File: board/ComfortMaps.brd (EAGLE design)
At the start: 96.8 x 49.3 mm, 47 parts, among them J1 PROG_HDR, U1 ADXL362, U3 ADP160-3.3, U4 MCP73833, X1 RASPI_GPIO_B+#_PIN

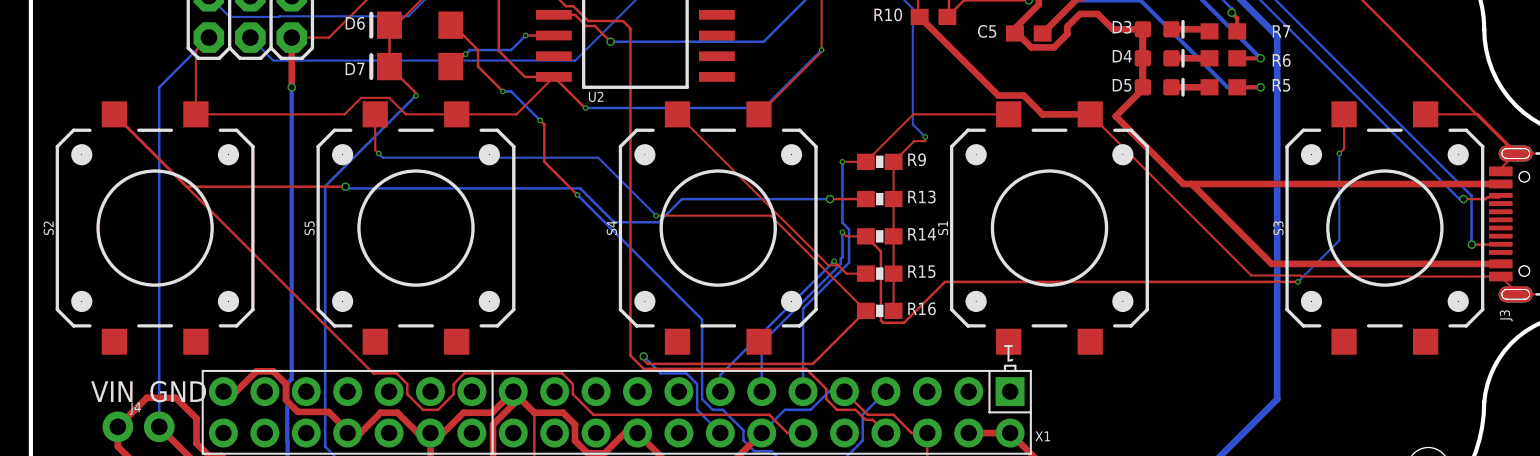
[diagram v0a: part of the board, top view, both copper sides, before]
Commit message: Enlarging spst button pads and connecting both sides.
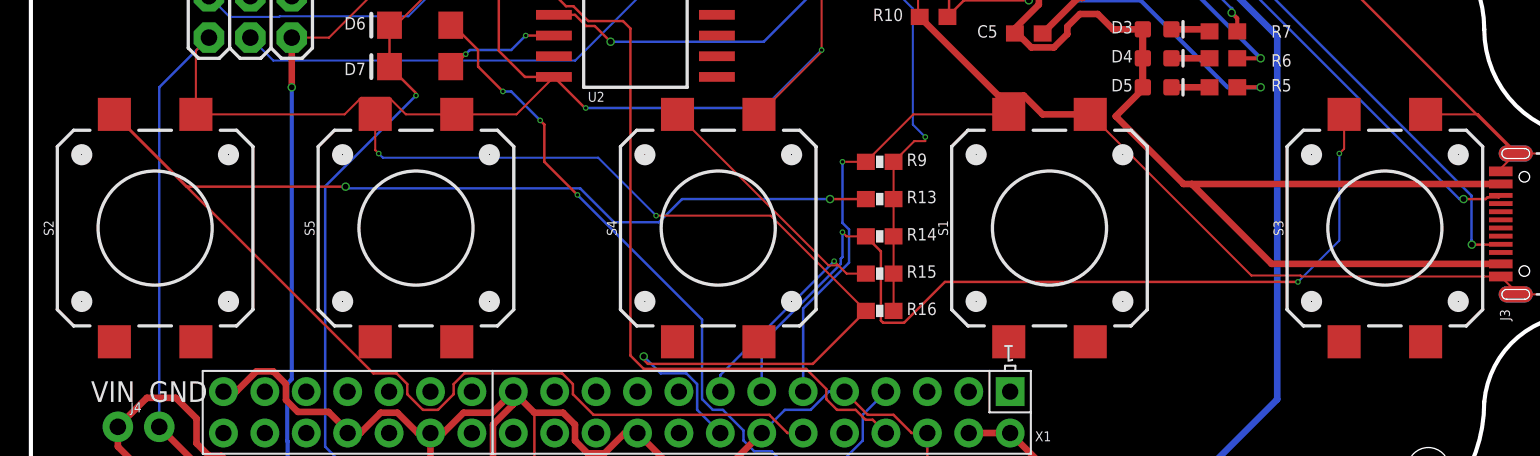
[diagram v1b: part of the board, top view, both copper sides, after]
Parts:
- S1, S2, S3, S4, S5: device SparkFun-Switches:TACTILE_SWITCH_SMD_12MM -> CM-SparkFun-Switches:TACTILE_SWITCH_SMD_12MM
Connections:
- net GND: now also S1.2, S2.2, S3.2, S4.2, S5.2
- net GPIO17: now also S1.4
- net GPIO18: now also S2.4
- net GPIO22: now also S4.4
- net GPIO23: now also S5.4
- net GPIO27: now also S3.4
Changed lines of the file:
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@@
 </element>
 <element name="U$3" library="SparkFun-Aesthetics" package="OSHW-LOGO-S" value="" x="6.274" y="0.279" smashed="yes" rot="R90"/>
-<element name="S1" library="SparkFun-Switches" library_urn="urn:adsk.eagle:library:535" package="TACTILE_SWITCH_SMD_12MM" package3d_urn="urn:adsk.eagle:package:40166/1" value="SPST-12MM" x="66.294" y="18.542" smashed="yes" rot="R90">
+<element name="S1" library="CM-SparkFun-Switches" package="TACTILE_SWITCH_SMD_12MM" value="SPST-12MM" x="66.294" y="18.542" smashed="yes" rot="R90">
 <attribute name="NAME" x="60.071" y="18.542" size="0.6096" layer="25" font="vector" ratio="20" rot="R90" align="bottom-center"/>
 <attribute name="PROD_ID" value="SWCH-11967" x="66.294" y="18.542" size="1.778" layer="27" rot="R90" display="off"/>
@@
 <attribute name="VALUE" x="72.517" y="18.542" size="0.6096" layer="27" font="vector" ratio="20" rot="R90" align="top-center"/>
 </element>
-<element name="S2" library="SparkFun-Switches" library_urn="urn:adsk.eagle:library:535" package="TACTILE_SWITCH_SMD_12MM" package3d_urn="urn:adsk.eagle:package:40166/1" override_package3d_urn="urn:adsk.eagle:package:15371983/2" override_package_urn="urn:adsk.eagle:footprint:40109/1" value="SPST-12MM" x="11.43" y="18.542" smashed="yes" rot="R90">
+<element name="S2" library="CM-SparkFun-Switches" package="TACTILE_SWITCH_SMD_12MM" override_package3d_urn="urn:adsk.eagle:package:15371983/2" override_package_urn="urn:adsk.eagle:footprint:40109/1" override_locally_modified="yes" value="SPST-12MM" x="11.43" y="18.542" smashed="yes" rot="R90">
 <attribute name="NAME" x="5.207" y="18.542" size="0.6096" layer="25" font="vector" ratio="20" rot="R90" align="bottom-center"/>
 <attribute name="PROD_ID" value="SWCH-11967" x="11.43" y="18.542" size="1.778" layer="27" rot="R90" display="off"/>
@@
 <attribute name="VALUE" x="17.653" y="18.542" size="0.6096" layer="27" font="vector" ratio="20" rot="R90" align="top-center"/>
 </element>
-<element name="S3" library="SparkFun-Switches" library_urn="urn:adsk.eagle:library:535" package="TACTILE_SWITCH_SMD_12MM" package3d_urn="urn:adsk.eagle:package:40166/1" value="SPST-12MM" x="86.868" y="18.542" smashed="yes" rot="R90">
+<element name="S3" library="CM-SparkFun-Switches" package="TACTILE_SWITCH_SMD_12MM" value="SPST-12MM" x="86.868" y="18.542" smashed="yes" rot="R90">
 <attribute name="NAME" x="80.645" y="18.542" size="0.6096" layer="25" font="vector" ratio="20" rot="R90" align="bottom-center"/>
 <attribute name="PROD_ID" value="SWCH-11967" x="86.868" y="18.542" size="1.778" layer="27" rot="R90" display="off"/>
@@
 <attribute name="VALUE" x="93.091" y="18.542" size="0.6096" layer="27" font="vector" ratio="20" rot="R90" align="top-center"/>
 </element>
-<element name="S4" library="SparkFun-Switches" library_urn="urn:adsk.eagle:library:535" package="TACTILE_SWITCH_SMD_12MM" package3d_urn="urn:adsk.eagle:package:40166/1" value="SPST-12MM" x="45.974" y="18.542" smashed="yes" rot="R90">
+<element name="S4" library="CM-SparkFun-Switches" package="TACTILE_SWITCH_SMD_12MM" value="SPST-12MM" x="45.974" y="18.542" smashed="yes" rot="R90">
 <attribute name="NAME" x="39.751" y="18.542" size="0.6096" layer="25" font="vector" ratio="20" rot="R90" align="bottom-center"/>
 <attribute name="PROD_ID" value="SWCH-11967" x="45.974" y="18.542" size="1.778" layer="27" rot="R90" display="off"/>
@@
 <attribute name="VALUE" x="52.197" y="18.542" size="0.6096" layer="27" font="vector" ratio="20" rot="R90" align="top-center"/>
 </element>
-<element name="S5" library="SparkFun-Switches" library_urn="urn:adsk.eagle:library:535" package="TACTILE_SWITCH_SMD_12MM" package3d_urn="urn:adsk.eagle:package:40166/1" value="SPST-12MM" x="27.432" y="18.542" smashed="yes" rot="R90">
+<element name="S5" library="CM-SparkFun-Switches" package="TACTILE_SWITCH_SMD_12MM" value="SPST-12MM" x="27.432" y="18.542" smashed="yes" rot="R90">
 <attribute name="NAME" x="21.209" y="18.542" size="0.6096" layer="25" font="vector" ratio="20" rot="R90" align="bottom-center"/>
 <attribute name="PROD_ID" value="SWCH-11967" x="27.432" y="18.542" size="1.778" layer="27" rot="R90" display="off"/>
@@
 <wire x1="35.14" y1="1.778" x2="34.6964" y2="2.2216" width="0.1524" layer="1"/>
 <wire x1="34.6964" y1="2.2216" x2="34.6964" y2="7.2136" width="0.1524" layer="1"/>
+<contactref element="S1" pad="2"/>
+<contactref element="S2" pad="2"/>
+<contactref element="S3" pad="2"/>
+<contactref element="S4" pad="2"/>
+<contactref element="S5" pad="2"/>
+<wire x1="93.98" y1="15.571" x2="89.368" y2="11.567" width="0" layer="19" extent="1-1"/>
+<wire x1="13.93" y1="11.567" x2="15.621" y2="8.509" width="0" layer="19" extent="1-1"/>
+<wire x1="29.932" y1="11.567" x2="33.401" y2="8.509" width="0" layer="19" extent="1-1"/>
+<wire x1="48.474" y1="11.567" x2="48.641" y2="5.969" width="0" layer="19" extent="1-1"/>
+<wire x1="68.794" y1="11.567" x2="58.801" y2="5.969" width="0" layer="19" extent="1-1"/>
 </signal>
 <signal name="OVERRIDE">
@@
 <wire x1="53.9988" y1="18.455675" x2="53.594" y2="18.860475" width="0.1524" layer="16"/>
 <wire x1="53.594" y1="18.860475" x2="53.594" y2="22.606" width="0.1524" layer="16"/>
+<contactref element="S1" pad="4"/>
+<wire x1="51.181" y1="8.509" x2="63.794" y2="11.567" width="0" layer="19" extent="1-1"/>
 </signal>
 <signal name="GPIO18">
@@
 <wire x1="23.114" y1="21.082" x2="13.365" y2="21.082" width="0.1524" layer="1"/>
 <wire x1="13.365" y1="21.082" x2="8.93" y2="25.517" width="0.1524" layer="1"/>
+<contactref element="S2" pad="4"/>
+<wire x1="8.93" y1="11.567" x2="8.93" y2="25.517" width="0" layer="19" extent="1-1"/>
 </signal>
 <signal name="GPIO27">
@@
 <wire x1="59.8812875" y1="15.24" x2="57.3746875" y2="12.7334" width="0.1524" layer="1"/>
 <wire x1="55.9514" y1="12.8673125" x2="55.9514" y2="17.1126" width="0.1524" layer="1"/>
+<contactref element="S3" pad="4"/>
+<wire x1="81.534" y1="15.24" x2="84.368" y2="11.567" width="0" layer="19" extent="1-1"/>
 </signal>
 <signal name="GPIO22">
@@
 <wire x1="53.086" y1="16.51" x2="46.101" y2="9.525" width="0.1524" layer="16"/>
 <wire x1="46.101" y1="9.525" x2="46.101" y2="8.509" width="0.1524" layer="16"/>
+<contactref element="S4" pad="4"/>
+<wire x1="43.474" y1="11.567" x2="46.101" y2="8.509" width="0" layer="19" extent="1-1"/>
 </signal>
 <signal name="GPIO23">
@@
 <wire x1="42.4434" y1="9.6266" x2="44.02393125" y2="9.6266" width="0.1524" layer="16"/>
 <wire x1="44.6786" y1="8.97193125" x2="44.6786" y2="7.3914" width="0.1524" layer="16"/>
+<contactref element="S5" pad="4"/>
+<wire x1="24.932" y1="11.567" x2="25.146" y2="23.114" width="0" layer="19" extent="1-1"/>
 </signal>
 <signal name="STAT1">

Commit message: Beginning v4 of board
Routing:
- net GND: track 356.4 -> 419.3 mm
- net GPIO17: track 26.8 -> 40.9 mm, vias 1 -> 2
- net GPIO18: track 102.7 -> 116.7 mm
- net GPIO23: track 59.2 -> 70.9 mm
- net GPIO22: track 26.9 -> 32.9 mm, vias 1 -> 2
- net GPIO27: track 57.0 -> 61.9 mm
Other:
- board text added: "Comfort Maps Samuel Clay V4 2020-02-28"
- board text removed: "Comfort Maps Samuel Clay V3 2020-01-27"
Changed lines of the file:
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@@
 <text x="8.382" y="35.56" size="1.524" layer="25" font="vector" ratio="20">Comfort Maps
 Samuel Clay
-V3 2020-01-27</text>
+V4 2020-02-28</text>
 <text x="51.689" y="0.127" size="1.016" layer="21" font="vector" ratio="15" rot="R180">WAKE</text>
 <text x="49.022" y="4.191" size="1.016" layer="21" font="vector" ratio="15" rot="R180">VOUT</text>
@@
 <wire x1="52.316" y1="34.8958" x2="52.316" y2="29.464" width="0.127" layer="1"/>
 <wire x1="52.316" y1="29.464" x2="52.316" y2="29.359" width="0.127" layer="1"/>
-<wire x1="52.316" y1="29.359" x2="48.474" y2="25.517" width="0.127" layer="1"/>
+<wire x1="52.316" y1="29.359" x2="48.5625" y2="25.6055" width="0.127" layer="1"/>
+<wire x1="48.5625" y1="25.6055" x2="48.474" y2="25.517" width="0.127" layer="1"/>
 <wire x1="54.7481" y1="35.4441" x2="54.7481" y2="36.1839" width="0.127" layer="1"/>
 <wire x1="54.1998" y1="34.8958" x2="54.7481" y2="35.4441" width="0.127" layer="1"/>
@@
 <wire x1="89.368" y1="25.517" x2="92.595" y2="25.517" width="0.127" layer="1"/>
 <wire x1="92.595" y1="25.517" x2="94.996" y2="23.116" width="0.127" layer="1"/>
-<wire x1="29.932" y1="25.517" x2="33.598" y2="25.517" width="0.127" layer="1"/>
+<wire x1="29.932" y1="25.517" x2="29.972" y2="25.517" width="0.127" layer="1"/>
+<wire x1="29.972" y1="25.517" x2="33.598" y2="25.517" width="0.127" layer="1"/>
 <wire x1="33.598" y1="25.517" x2="35.894" y2="27.813" width="0.127" layer="1"/>
 <wire x1="14.732" y1="30.226" x2="13.93" y2="29.424" width="0.127" layer="1"/>
 <wire x1="13.93" y1="25.517" x2="13.93" y2="29.424" width="0.127" layer="1"/>
-<wire x1="24.06756875" y1="26.5329" x2="25.79643125" y2="26.5329" width="0.127" layer="1"/>
-<wire x1="13.93" y1="25.517" x2="23.05166875" y2="25.517" width="0.127" layer="1"/>
-<wire x1="26.81233125" y1="25.517" x2="29.932" y2="25.517" width="0.127" layer="1"/>
-<wire x1="23.05166875" y1="25.517" x2="24.06756875" y2="26.5329" width="0.127" layer="1"/>
-<wire x1="25.79643125" y1="26.5329" x2="26.81233125" y2="25.517" width="0.127" layer="1"/>
+<wire x1="23.55956875" y1="26.7869" x2="26.05043125" y2="26.7869" width="0.127" layer="1"/>
+<wire x1="13.93" y1="25.517" x2="22.28966875" y2="25.517" width="0.127" layer="1"/>
+<wire x1="27.32033125" y1="25.517" x2="29.932" y2="25.517" width="0.127" layer="1"/>
+<wire x1="22.28966875" y1="25.517" x2="23.55956875" y2="26.7869" width="0.127" layer="1"/>
+<wire x1="26.05043125" y1="26.7869" x2="27.32033125" y2="25.517" width="0.127" layer="1"/>
 <wire x1="21.0166" y1="-2.17439375" x2="20.65099375" y2="-2.54" width="0.4064" layer="1"/>
 <wire x1="20.65099375" y1="-2.54" x2="19.86700625" y2="-2.54" width="0.4064" layer="1"/>
@@
 <wire x1="62.484" y1="37.084" x2="62.396" y2="36.996" width="0.4064" layer="1"/>
 <wire x1="62.396" y1="36.996" x2="62.396" y2="36.576" width="0.4064" layer="1"/>
-<wire x1="64.71629375" y1="26.6726" x2="63.1554" y2="26.6726" width="0.4064" layer="1"/>
-<wire x1="63.1554" y1="26.6726" x2="58.249" y2="31.579" width="0.4064" layer="1"/>
-<wire x1="68.794" y1="25.517" x2="65.87189375" y2="25.517" width="0.4064" layer="1"/>
-<wire x1="65.87189375" y1="25.517" x2="64.71629375" y2="26.6726" width="0.4064" layer="1"/>
+<wire x1="65.22429375" y1="27.4346" x2="62.3934" y2="27.4346" width="0.4064" layer="1"/>
+<wire x1="62.3934" y1="27.4346" x2="58.249" y2="31.579" width="0.4064" layer="1"/>
+<wire x1="68.794" y1="25.517" x2="67.14189375" y2="25.517" width="0.4064" layer="1"/>
+<wire x1="67.14189375" y1="25.517" x2="65.22429375" y2="27.4346" width="0.4064" layer="1"/>
 <wire x1="28.321" y1="3.683" x2="26.885" y2="2.247" width="0.4064" layer="1"/>
 <wire x1="28.321" y1="3.683" x2="28.321" y2="5.969" width="0.4064" layer="1"/>
@@
 <contactref element="S4" pad="2"/>
 <contactref element="S5" pad="2"/>
-<wire x1="93.98" y1="15.571" x2="89.368" y2="11.567" width="0" layer="19" extent="1-1"/>
-<wire x1="13.93" y1="11.567" x2="15.621" y2="8.509" width="0" layer="19" extent="1-1"/>
-<wire x1="29.932" y1="11.567" x2="33.401" y2="8.509" width="0" layer="19" extent="1-1"/>
-<wire x1="48.474" y1="11.567" x2="48.641" y2="5.969" width="0" layer="19" extent="1-1"/>
-<wire x1="68.794" y1="11.567" x2="58.801" y2="5.969" width="0" layer="19" extent="1-1"/>
+<wire x1="13.93" y1="11.567" x2="15.621" y2="9.876" width="0.1524" layer="1"/>
+<wire x1="15.621" y1="9.876" x2="15.621" y2="8.509" width="0.1524" layer="1"/>
+<wire x1="29.932" y1="11.567" x2="29.932" y2="25.477" width="0.1524" layer="1"/>
+<wire x1="29.932" y1="25.477" x2="29.972" y2="25.517" width="0.1524" layer="1"/>
+<wire x1="48.474" y1="11.567" x2="48.474" y2="11.724" width="0.1524" layer="1"/>
+<wire x1="48.474" y1="11.724" x2="41.148" y2="19.05" width="0.1524" layer="1"/>
+<wire x1="41.148" y1="19.05" x2="41.148" y2="26.416" width="0.1524" layer="1"/>
+<wire x1="41.148" y1="26.416" x2="41.91" y2="27.178" width="0.1524" layer="1"/>
+<wire x1="41.91" y1="27.178" x2="46.99" y2="27.178" width="0.1524" layer="1"/>
+<wire x1="46.99" y1="27.178" x2="48.5625" y2="25.6055" width="0.1524" layer="1"/>
+<wire x1="68.794" y1="11.567" x2="64.9986" y2="7.7716" width="0.1524" layer="1"/>
+<wire x1="64.9986" y1="7.7716" x2="64.9986" y2="7.5253125" width="0.1524" layer="1"/>
+<wire x1="59.76046875" y1="5.969" x2="58.801" y2="5.969" width="0.1524" layer="1"/>
+<wire x1="60.87806875" y1="7.0866" x2="59.76046875" y2="5.969" width="0.1524" layer="1"/>
+<wire x1="64.9986" y1="7.5253125" x2="64.5598875" y2="7.0866" width="0.1524" layer="1"/>
+<wire x1="64.5598875" y1="7.0866" x2="60.87806875" y2="7.0866" width="0.1524" layer="1"/>
+<wire x1="89.368" y1="11.567" x2="93.372" y2="15.571" width="0.1524" layer="1"/>
+<wire x1="93.372" y1="15.571" x2="93.98" y2="15.571" width="0.1524" layer="1"/>
 </signal>
 <signal name="OVERRIDE">
@@
 <wire x1="53.594" y1="18.860475" x2="53.594" y2="22.606" width="0.1524" layer="16"/>
 <contactref element="S1" pad="4"/>
-<wire x1="51.181" y1="8.509" x2="63.794" y2="11.567" width="0" layer="19" extent="1-1"/>
+<wire x1="63.794" y1="11.567" x2="57.033" y2="11.567" width="0.1524" layer="1"/>
+<wire x1="57.033" y1="11.567" x2="56.388" y2="10.922" width="0.1524" layer="1"/>
+<wire x1="56.388" y1="10.922" x2="56.388" y2="10.668" width="0.1524" layer="1"/>
+<via x="56.388" y="10.668" extent="1-16" drill="0.35"/>
+<wire x1="56.388" y1="10.668" x2="53.34" y2="10.668" width="0.1524" layer="16"/>
+<wire x1="53.34" y1="10.668" x2="51.181" y2="8.509" width="0.1524" layer="16"/>
 </signal>
 <signal name="GPIO18">
@@
 <wire x1="13.365" y1="21.082" x2="8.93" y2="25.517" width="0.1524" layer="1"/>
 <contactref element="S2" pad="4"/>
-<wire x1="8.93" y1="11.567" x2="8.93" y2="25.517" width="0" layer="19" extent="1-1"/>
+<wire x1="8.93" y1="11.567" x2="8.93" y2="25.517" width="0.1524" layer="1"/>
 </signal>
 <signal name="GPIO27">
@@
 <wire x1="55.9514" y1="12.8673125" x2="55.9514" y2="17.1126" width="0.1524" layer="1"/>
 <contactref element="S3" pad="4"/>
-<wire x1="81.534" y1="15.24" x2="84.368" y2="11.567" width="0" layer="19" extent="1-1"/>
+<wire x1="84.368" y1="11.567" x2="81.534" y2="14.401" width="0.1524" layer="1"/>
+<wire x1="81.534" y1="14.401" x2="81.534" y2="15.24" width="0.1524" layer="1"/>
 </signal>
 <signal name="GPIO22">
@@
 <wire x1="46.101" y1="9.525" x2="46.101" y2="8.509" width="0.1524" layer="16"/>
 <contactref element="S4" pad="4"/>
-<wire x1="43.474" y1="11.567" x2="46.101" y2="8.509" width="0" layer="19" extent="1-1"/>
+<wire x1="43.474" y1="11.567" x2="43.591" y2="11.684" width="0.1524" layer="1"/>
+<via x="46.228" y="11.684" extent="1-16" drill="0.35"/>
+<wire x1="46.228" y1="11.684" x2="46.228" y2="8.636" width="0.1524" layer="16"/>
+<wire x1="46.228" y1="8.636" x2="46.101" y2="8.509" width="0.1524" layer="16"/>
+<wire x1="43.591" y1="11.684" x2="46.228" y2="11.684" width="0.1524" layer="1"/>
 </signal>
 <signal name="GPIO23">
@@
 <wire x1="44.6786" y1="8.97193125" x2="44.6786" y2="7.3914" width="0.1524" layer="16"/>
 <contactref element="S5" pad="4"/>
-<wire x1="24.932" y1="11.567" x2="25.146" y2="23.114" width="0" layer="19" extent="1-1"/>
+<wire x1="24.932" y1="11.567" x2="24.932" y2="22.9" width="0.1524" layer="1"/>
+<wire x1="24.932" y1="22.9" x2="25.146" y2="23.114" width="0.1524" layer="1"/>
 </signal>
 <signal name="STAT1">
